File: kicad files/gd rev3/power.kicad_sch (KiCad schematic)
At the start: 3 parts, among them U18 LM7905_TO220

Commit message: poking around with the laying
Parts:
- added C52, C53: 1u, Capacitor_SMD:C_0805_2012Metric, symbol Device:C
- added Cf1, Cf2, Cf3: 100n, Capacitor_SMD:C_0805_2012Metric, symbol My_Library:C_0805
- added Cin1, Cin2, Cin3: 300u, Capacitor_SMD:CP_Elec_8x10.5, symbol My_Library:C_0805
- added Co1, Co2, Co3: 4700u, Capacitor_SMD:CP_Elec_18x17.5, symbol My_Library:C_0805
- added D4, D5, D6: 50V,5A, Diode_SMD:D_SMC, symbol Device:D_Schottky_Small
- added J18: VIN_Jack, Connector_BarrelJack:BarrelJack_Horizontal, symbol Connector:Barrel_Jack_Switch
- added L1, L2, L3: 180u, Inductor_SMD:L_Bourns_SRR1210A, symbol Device:L_Small
- added R42, R45: k, Resistor_SMD:R_0805_2012Metric, symbol My_Library:R_0805
- added R43, R44, R46: 6.8k, Resistor_SMD:R_0805_2012Metric, symbol My_Library:R_0805
- added Rf1, Rf2, Rf3: 68k, Resistor_SMD:R_0805_2012Metric, symbol My_Library:R_0805
- added SW7: POWER-Change Footprint, Connector_PinHeader_2.54mm:PinHeader_1x02_P2.54mm_Vertical, symbol Switch:SW_SPST
- added TP10, TP11, TP15: Out, My Libraries:Harwin-S1751-46-Test-Point, symbol Connector:TestPoint
- added TP12, TP4, TP5: In, My Libraries:Harwin-S1751-46-Test-Point, symbol Connector:TestPoint
- added TP13, TP6, TP7: FB, My Libraries:Harwin-S1751-46-Test-Point, symbol Connector:TestPoint
- added TP14, TP8, TP9: SW, My Libraries:Harwin-S1751-46-Test-Point, symbol Connector:TestPoint
- added U21, U23, U24: MC34167, Package_TO_SOT_THT:TO-220-5_P3.4x3.7mm_StaggerOdd_Lead3.8mm_Vertical, symbol My_Library:MC34167
- added U25: MIC5504-3.3YM5, Package_TO_SOT_SMD:SOT-23-5, symbol Regulator_Linear:MIC5504-3.3YM5
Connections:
- net -12V: now also Co2.1, L2.2, R44.1, TP11.1
- net GND: now also C52.2, C53.2, Cin1.2, Cin2.2, Cin3.2, Co1.2, Co2.2, Co3.2, D4.2 (A), D5.2 (A), D6.2 (A), J18.2, J18.3, R42.2, R45.2, U21.3 (GND), U23.3 (GND), U24.3 (GND), U25.2 (GND)
- new net: Cf2.2, Rf2.2
- new net: Cf3.2, Rf3.2
- new net: Cf1.2, Rf1.2
- new net +12V: Co3.1, L3.2, R46.1, TP15.1
- new net +3V3: C53.1, U25.5 (VOUT)
- new net +5V: C52.1, Co1.1, L1.2, R43.1, TP10.1, U25.1 (VIN), U25.3 (EN)
- new net Comp: Cf1.1, Cf2.1, Cf3.1, U21.5 (Comp), U23.5 (Comp), U24.5 (Comp)
- new net Fb: R42.1, R43.2, R44.2, R45.1, R46.2, Rf1.1, Rf2.1, Rf3.1, TP13.1, TP6.1, TP7.1, U21.1 (Vfb), U23.1 (Vfb), U24.1 (Vfb)
- new net SW: D4.1 (K), D5.1 (K), D6.1 (K), L1.1, L2.1, L3.1, TP14.1, TP8.1, TP9.1, U21.2 (Out), U23.2 (Out), U24.2 (Out)
- new net Vin: Cin1.1, Cin2.1, Cin3.1, SW7.2 (B), TP12.1, TP4.1, TP5.1, U21.4 (In), U23.4 (In), U24.4 (In)
- new net Vraw: J18.1, SW7.1 (A)
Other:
- note added: "Change to SMD Package (if you can buy it)"
- note added: "Incorrect Circuit"
- note added: "Incorrect Feedback Values"
- note added: "LDO for 15V to 5V for "standby" of the keyboard RP2040"
- moved on the sheet: C35, C36, U18

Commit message: KBD Video and Power sheet labels, initial create
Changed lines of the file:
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@@
+    (stroke (width 0) (type default) (color 0 0 0 0))
+  )
+  (wire (pts (xy 31.75 135.89) (xy 44.45 135.89))
     (stroke (width 0) (type default) (color 0 0 0 0))
   )
@@
     (stroke (width 0) (type default) (color 0 0 0 0))
   )
+  (wire (pts (xy 31.75 133.35) (xy 44.45 133.35))
+    (stroke (width 0) (type default) (color 0 0 0 0))
+  )
   (wire (pts (xy 106.68 49.53) (xy 109.22 49.53))
     (stroke (width 0) (type default) (color 0 0 0 0))
@@
     (stroke (width 0) (type default) (color 0 0 0 0))
   )
+  (wire (pts (xy 31.75 128.27) (xy 44.45 128.27))
+    (stroke (width 0) (type default) (color 0 0 0 0))
+  )
   (wire (pts (xy 193.04 72.39) (xy 193.04 68.58))
     (stroke (width 0) (type default) (color 0 0 0 0))
@@
   )
   (wire (pts (xy 187.96 115.57) (xy 184.15 115.57))
+    (stroke (width 0) (type default) (color 0 0 0 0))
+  )
+  (wire (pts (xy 31.75 130.81) (xy 44.45 130.81))
     (stroke (width 0) (type default) (color 0 0 0 0))
   )
@@
     (effects (font (size 1.27 1.27)) (justify left bottom))
   )
+  (label "+12V_Enable" (at 44.45 130.81 180)
+    (effects (font (size 1.27 1.27)) (justify right bottom))
+  )
+  (label "+5V_Enable" (at 44.45 128.27 180)
+    (effects (font (size 1.27 1.27)) (justify right bottom))
+  )
+  (label "MEGA_PWR" (at 44.45 135.89 180)
+    (effects (font (size 1.27 1.27)) (justify right bottom))
+  )
   (label "Fb" (at 189.23 66.04 180)
     (effects (font (size 1.27 1.27)) (justify right bottom))
@@
     (effects (font (size 1.27 1.27)) (justify right bottom))
   )
+  (label "-12V_Enable" (at 44.45 133.35 180)
+    (effects (font (size 1.27 1.27)) (justify right bottom))
+  )
   (label "Fb" (at 113.03 128.27 180)
     (effects (font (size 1.27 1.27)) (justify right bottom))
@@
     (effects (font (size 1.27 1.27)) (justify left bottom))
   )
+  (hierarchical_label "-12V_Enable" (shape input) (at 31.75 133.35 180)
+    (effects (font (size 1.27 1.27)) (justify right))
+  )
+  (hierarchical_label "+5V_Enable" (shape input) (at 31.75 128.27 180)
+    (effects (font (size 1.27 1.27)) (justify right))
+  )
+  (hierarchical_label "+12V_Enable" (shape input) (at 31.75 130.81 180)
+    (effects (font (size 1.27 1.27)) (justify right))
+  )
+  (hierarchical_label "MEGA_PWR" (shape input) (at 31.75 135.89 180)
+    (effects (font (size 1.27 1.27)) (justify right))
+  )
   (symbol (lib_id "power:-5V") (at 187.96 114.3 0) (unit 1)

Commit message: added missing Flash to 2040 circuits and sync'd title blocks
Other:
- company: (none) -> twitch.tv/baldengineer
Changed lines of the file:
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@@
 (kicad_sch (version 20211123) (generator eeschema)
   (paper "A4")
+  (title_block
+    (rev "3a")
+    (company "twitch.tv/baldengineer")
+  )
   (junction (at 157.48 49.53) (diameter 0) (color 0 0 0 0)
   )

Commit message: on-stream clean-up work
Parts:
- removed C35, C36: 10u, Capacitor_SMD:C_0805_2012Metric, symbol My_Library:C_0805
- removed C52, C53: 1u, Capacitor_SMD:C_0805_2012Metric, symbol Device:C
- removed Cf1, Cf2, Cf3: 100n, Capacitor_SMD:C_0805_2012Metric, symbol My_Library:C_0805
- removed Cin1, Cin2, Cin3: 300u, Capacitor_SMD:CP_Elec_8x10.5, symbol My_Library:C_0805
- removed Co1, Co2, Co3: 4700u, Capacitor_SMD:CP_Elec_18x17.5, symbol My_Library:C_0805
- removed D4, D5, D6: 50V,5A, Diode_SMD:D_SMC, symbol Device:D_Schottky_Small
- removed J18: VIN_Jack, Connector_BarrelJack:BarrelJack_Horizontal, symbol Connector:Barrel_Jack_Switch
- removed L1, L2, L3: 180u, Inductor_SMD:L_Bourns_SRR1210A, symbol Device:L_Small
- removed R42, R45: k, Resistor_SMD:R_0805_2012Metric, symbol My_Library:R_0805
- removed R43, R44, R46: 6.8k, Resistor_SMD:R_0805_2012Metric, symbol My_Library:R_0805
- removed Rf1, Rf2, Rf3: 68k, Resistor_SMD:R_0805_2012Metric, symbol My_Library:R_0805
- removed SW7: POWER-Change Footprint, Connector_PinHeader_2.54mm:PinHeader_1x02_P2.54mm_Vertical, symbol Switch:SW_SPST
- removed TP10, TP11, TP15: Out, My Libraries:Harwin-S1751-46-Test-Point, symbol Connector:TestPoint
- removed TP12, TP4, TP5: In, My Libraries:Harwin-S1751-46-Test-Point, symbol Connector:TestPoint
- removed TP13, TP6, TP7: FB, My Libraries:Harwin-S1751-46-Test-Point, symbol Connector:TestPoint
- removed TP14, TP8, TP9: SW, My Libraries:Harwin-S1751-46-Test-Point, symbol Connector:TestPoint
- removed U18: LM7905_TO220, Package_TO_SOT_THT:TO-220-3_Vertical, symbol Regulator_Linear:LM7905_TO220
- removed U21, U23, U24: MC34167, Package_TO_SOT_THT:TO-220-5_P3.4x3.7mm_StaggerOdd_Lead3.8mm_Vertical, symbol My_Library:MC34167
- removed U25: MIC5504-3.3YM5, Package_TO_SOT_SMD:SOT-23-5, symbol Regulator_Linear:MIC5504-3.3YM5
- added D10: Stby, LED_SMD:LED_0805_2012Metric, symbol My Library:D_1206
- added D4: -12v, LED_SMD:LED_0805_2012Metric, symbol My Library:D_1206
- added D5: +12v, LED_SMD:LED_0805_2012Metric, symbol My Library:D_1206
- added D6: Mega, LED_SMD:LED_0805_2012Metric, symbol My Library:D_1206
- added J12: Right Angle, My Libraries:TE 5650118-3 Right Angle 12 Pos Socket, symbol Connector_Generic:Conn_02x06_Odd_Even
- added J15: Rev2 Header, Connector_PinSocket_2.54mm:PinSocket_2x04_P2.54mm_Vertical, symbol Connector_Generic:Conn_02x04_Odd_Even
- added J16: RP2040 Header, Connector_PinSocket_2.54mm:PinSocket_2x03_P2.54mm_Vertical, symbol Connector_Generic:Conn_02x03_Odd_Even
- added R27, R28, R29, R30: 1K, Resistor_SMD:R_0805_2012Metric, symbol My Library:R_0805
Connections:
- net GND: now also D10.1 (K), D5.1 (K), D6.1 (K), J12.2 (Pin_2), J12.4 (Pin_4), J12.6 (Pin_6), J12.8 (Pin_8), J15.1 (Pin_1), J15.2 (Pin_2), J16.3 (Pin_3), J16.4 (Pin_4), R27.1
- new net: D5.2 (A), R28.2
- new net: D10.2 (A), R30.2
- new net: D6.2 (A), R29.2
- new net: D4.2 (A), R27.2
- new net Analog_En: J12.12 (Pin_12), J16.1 (Pin_1)
- new net Mega_En: J12.11 (Pin_11), J16.2 (Pin_2)
- new net Neg12: D4.1 (K), J12.1 (Pin_1), J15.7 (Pin_7), J15.8 (Pin_8)
- new net Pos12: J12.3 (Pin_3), J15.5 (Pin_5), J15.6 (Pin_6), R28.1
- new net mega_5v: J12.7 (Pin_7), J15.3 (Pin_3), J15.4 (Pin_4), R29.1
- new net stb_5v: J12.5 (Pin_5), J16.5 (Pin_5), J16.6 (Pin_6), R30.1
- no-connect marks 0 -> 2
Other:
- note added: "Change PWR Control Signals to Match Mega_EN Analog_EN"
- note removed: "Incorrect Circuit"
- note removed: "Incorrect Feedback Values"
- note removed: "LDO for 15V to 5V for "standby" of the keyboard RP2040"

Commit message: ERC clean-up
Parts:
- D10, D4, D5, D6: footprint LED_SMD:LED_0805_2012Metric -> LED_SMD:LED_1206_3216Metric
- J15: footprint Connector_PinSocket_2.54mm:PinSocket_2x04_P2.54mm_Vertical -> Connector_PinSocket_2.54mm:PinSocket_2x05_P2.54mm_Vertical; symbol Connector_Generic:Conn_02x04_Odd_Even -> Connector_Generic:Conn_02x05_Odd_Even
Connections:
- net GND: now also J15.10 (Pin_10), J15.9 (Pin_9); no longer J15.1 (Pin_1), J15.2 (Pin_2)
- net Neg12: now also J15.1 (Pin_1), J15.2 (Pin_2); no longer D4.1 (K), J15.7 (Pin_7), J15.8 (Pin_8)
- net Pos12: now also J15.3 (Pin_3), J15.4 (Pin_4); no longer J15.5 (Pin_5), J15.6 (Pin_6), R28.1
- net mega_5v: now also J15.7 (Pin_7), J15.8 (Pin_8); no longer J15.3 (Pin_3), J15.4 (Pin_4)
- net stb_5v: now also J15.5 (Pin_5), J15.6 (Pin_6)
- net Analog_En renamed Analog_Pwr
- net Mega_En renamed Mega_Pwr
- new net Neg12_Out: D4.1 (K)
- new net Pos12_Out: R28.1
- no-connect marks 2 -> 0

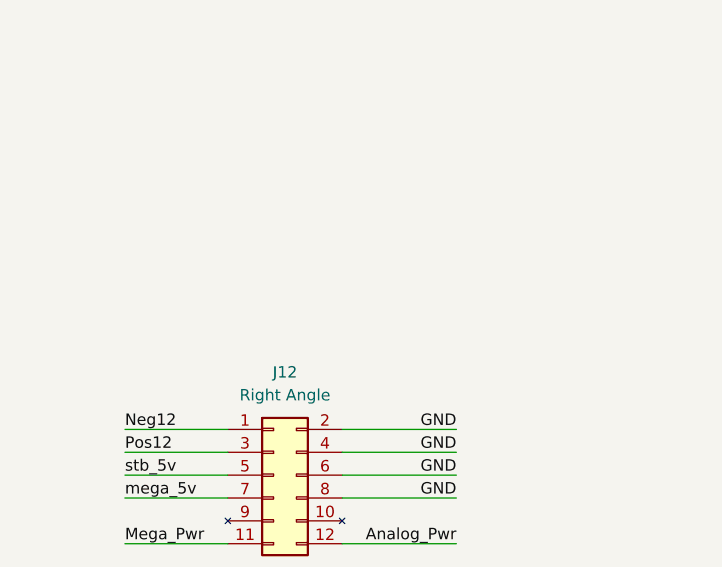
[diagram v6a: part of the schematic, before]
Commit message: Rough routing Main Data to figure out PCB floorplan.
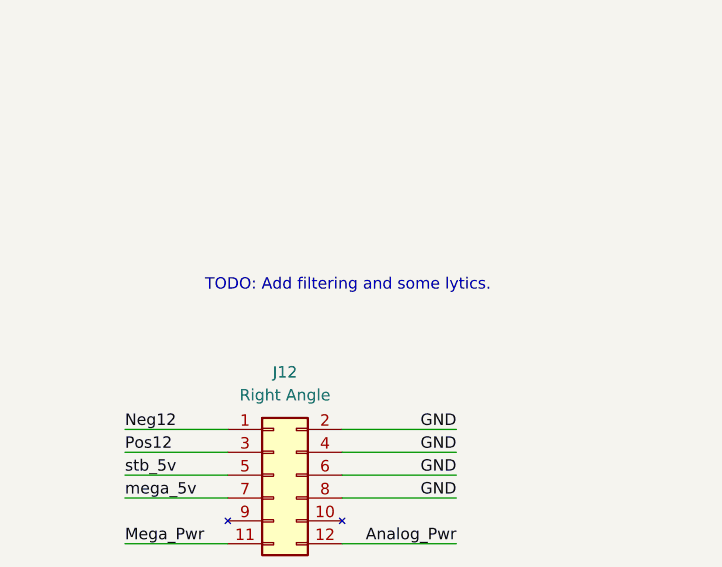
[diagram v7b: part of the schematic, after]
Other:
- note added: "TODO: Add filtering and some lytics."
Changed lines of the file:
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@@
+    (effects (font (size 1.27 1.27)) (justify left bottom))
+  )
+  (text "TODO: Add filtering and some lytics." (at 125.73 68.58 0)
     (effects (font (size 1.27 1.27)) (justify left bottom))
   )

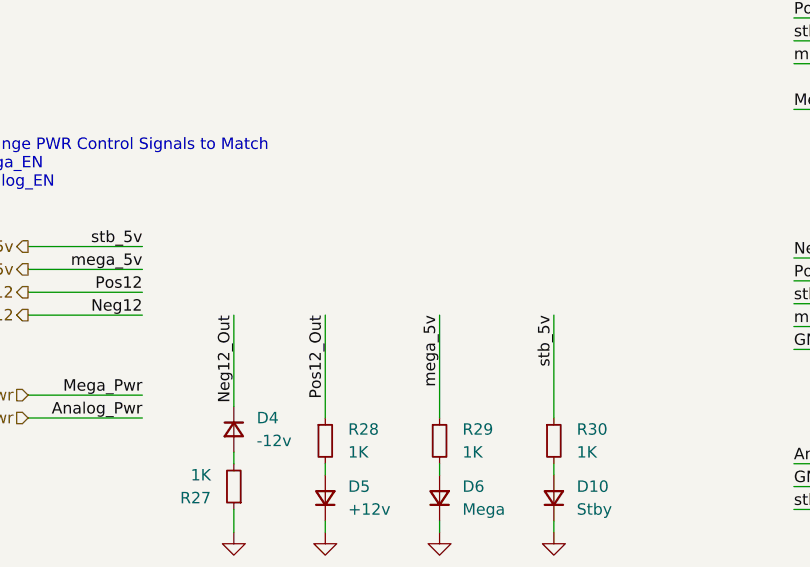
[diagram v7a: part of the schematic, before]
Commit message: 95: 5V (mega logic) routed/wired.
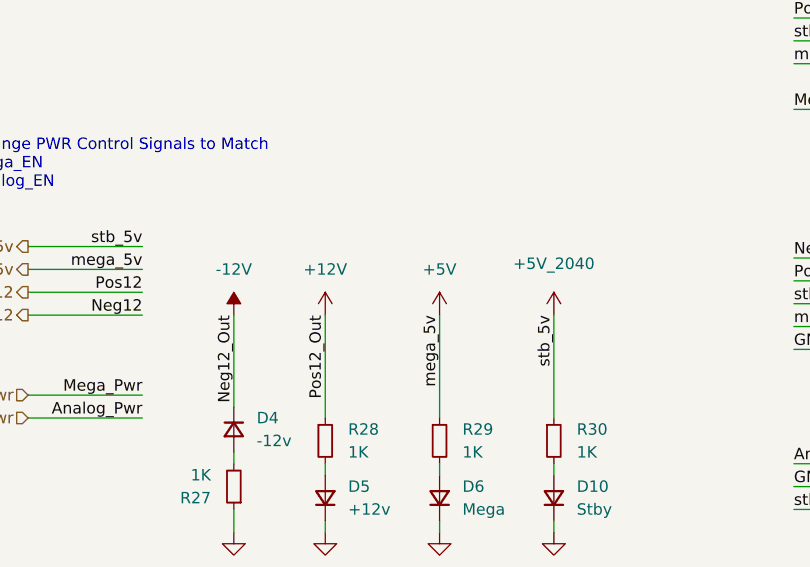
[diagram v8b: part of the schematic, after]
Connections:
- net Neg12_Out renamed -12V
- net Pos12_Out renamed +12V
- net mega_5v renamed +5V
- net stb_5v renamed +5V_2040
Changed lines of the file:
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@@
     (pin "2")
+  )
+  (symbol (lib_id "power:+12V") (at 64.77 119.38 0) (unit 1)
+    (in_bom yes) (on_board yes) (fields_autoplaced)
+    (property "Reference" "#PWR0392" (id 0) (at 64.77 123.19 0)
+      (effects (font (size 1.27 1.27)) hide)
+    )
+    (property "Value" "+12V" (id 1) (at 64.77 114.3 0))
+    (property "Footprint" "" (id 2) (at 64.77 119.38 0)
+      (effects (font (size 1.27 1.27)) hide)
+    )
+    (property "Datasheet" "" (id 3) (at 64.77 119.38 0)
+      (effects (font (size 1.27 1.27)) hide)
+    )
+    (pin "1")
   )
   (symbol (lib_id "My Library:D_1206") (at 54.61 132.08 270) (unit 1)
@@
     )
     (property "Datasheet" "" (id 3) (at 90.17 143.51 0)
+      (effects (font (size 1.27 1.27)) hide)
+    )
+    (pin "1")
+  )
+  (symbol (lib_id "power:+5V") (at 77.47 119.38 0) (unit 1)
+    (in_bom yes) (on_board yes) (fields_autoplaced)
+    (property "Reference" "#PWR0391" (id 0) (at 77.47 123.19 0)
+      (effects (font (size 1.27 1.27)) hide)
+    )
+    (property "Value" "+5V" (id 1) (at 77.47 114.3 0))
+    (property "Footprint" "" (id 2) (at 77.47 119.38 0)
+      (effects (font (size 1.27 1.27)) hide)
+    )
+    (property "Datasheet" "" (id 3) (at 77.47 119.38 0)
       (effects (font (size 1.27 1.27)) hide)
     )
@@
     (pin "2")
   )
+  (symbol (lib_id "My Library:+5V_2040") (at 90.17 119.38 0) (unit 1)
+    (in_bom yes) (on_board yes) (fields_autoplaced)
+    (property "Reference" "#PWR0390" (id 0) (at 90.17 123.19 0)
+      (effects (font (size 1.27 1.27)) hide)
+    )
+    (property "Value" "+5V_2040" (id 1) (at 90.17 113.665 0))
+    (property "Footprint" "" (id 2) (at 90.17 119.38 0)
+      (effects (font (size 1.27 1.27)) hide)
+    )
+    (property "Datasheet" "" (id 3) (at 90.17 119.38 0)
+      (effects (font (size 1.27 1.27)) hide)
+    )
+    (pin "1")
+  )
   (symbol (lib_id "My Library:D_1206") (at 64.77 139.7 90) (unit 1)
     (in_bom yes) (on_board yes) (fields_autoplaced)
@@
     (pin "2")
   )
+  (symbol (lib_id "power:-12V") (at 54.61 119.38 0) (unit 1)
+    (in_bom yes) (on_board yes) (fields_autoplaced)
+    (property "Reference" "#PWR0402" (id 0) (at 54.61 116.84 0)
+      (effects (font (size 1.27 1.27)) hide)
+    )
+    (property "Value" "-12V" (id 1) (at 54.61 114.3 0))
+    (property "Footprint" "" (id 2) (at 54.61 119.38 0)
+      (effects (font (size 1.27 1.27)) hide)
+    )
+    (property "Datasheet" "" (id 3) (at 54.61 119.38 0)
+      (effects (font (size 1.27 1.27)) hide)
+    )
+    (pin "1")
+  )
 )
